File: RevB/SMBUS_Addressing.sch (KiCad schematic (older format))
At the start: 16 parts, among them SW1 SW_DIP_x03, SW2 SW_DIP_x04, SW3 SW_DIP_x03, U3 4051

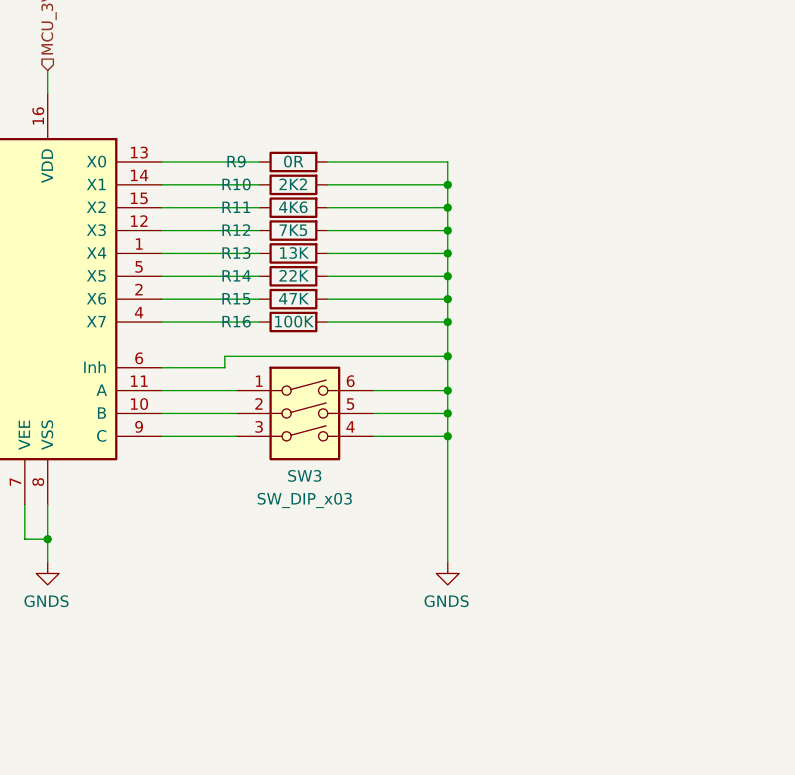
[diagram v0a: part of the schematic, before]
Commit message: updated revb
added missing pullup resistors
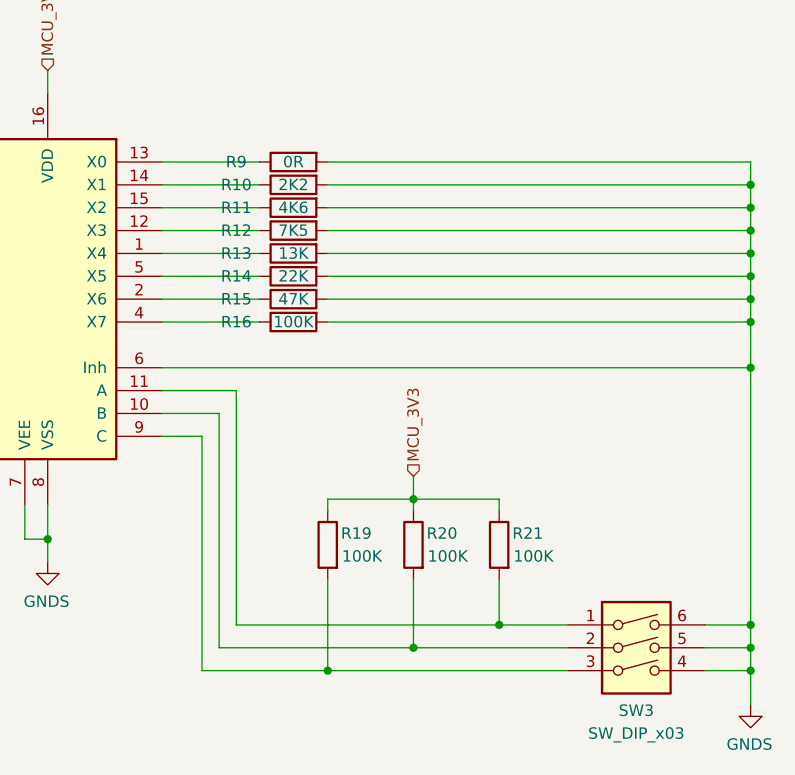
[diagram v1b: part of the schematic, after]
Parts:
- added R19, R20, R21: 100K, Resistor_SMD:R_0805_2012Metric_Pad1.15x1.40mm_HandSolder, symbol Device:R
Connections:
- net MCU_3V3: now also R19.1, R20.1, R21.1
- net at SW3.1, U3.11 (A): now also R21.2
- net at SW3.2, U3.10 (B): now also R20.2
- net at SW3.3, U3.9 (C): now also R19.2
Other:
- moved on the sheet: SW3
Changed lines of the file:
@@
 F 1 "4051" H 6094 4330 50  0000 L CNN
 F 2 "Package_SO:SOIC-16_3.9x9.9mm_P1.27mm" H 5550 4375 50  0001 C CNN
-F 3 "http://www.intersil.com/content/dam/Intersil/documents/cd40/cd4051bms-52bms-53bms.pdf" H 5550 4375 50  0001 C CNN
+F 3 "https://www.ti.com/lit/ds/symlink/cd4052b.pdf?ts=1595798534897&ref_url=https%253A%252F%252Fwww.google.com%252F" H 5550 4375 50  0001 C CNN
 	1    5550 4375
 	-1   0    0    -1
@@
 Wire Wire Line
 	5550 5425 5550 5525
-Wire Wire Line
-	6375 4775 6050 4775
-Wire Wire Line
-	6050 4875 6375 4875
-Wire Wire Line
-	6375 4975 6050 4975
 $Comp
 L power:GNDS #PWR?
 U 1 1 5F3F82F4
-P 7300 5525
+P 8625 6150
 AR Path="/5EFF0F4B/5F3F82F4" Ref="#PWR?"  Part="1"
 AR Path="/5F02F4E9/5F3E7977/5F3F82F4" Ref="#PWR08"  Part="1"
 AR Path="/5F02F4E9/5F4AA6E5/5F3F82F4" Ref="#PWR013"  Part="1"
-F 0 "#PWR013" H 7300 5275 50  0001 C CNN
-F 1 "GNDS" H 7305 5352 50  0000 C CNN
-F 2 "" H 7300 5525 50  0001 C CNN
-F 3 "" H 7300 5525 50  0001 C CNN
-	1    7300 5525
-	-1   0    0    -1
-$EndComp
-Wire Wire Line
-	7300 4975 6975 4975
-Wire Wire Line
-	6975 4875 7300 4875
-Wire Wire Line
-	7300 4875 7300 4975
-Connection ~ 7300 4975
-Wire Wire Line
-	7300 4975 7300 5525
-Wire Wire Line
-	6975 4775 7300 4775
-Wire Wire Line
-	7300 4775 7300 4875
-Connection ~ 7300 4875
-Connection ~ 7300 4775
+F 0 "#PWR013" H 8625 5900 50  0001 C CNN
+F 1 "GNDS" H 8630 5977 50  0000 C CNN
+F 2 "" H 8625 6150 50  0001 C CNN
+F 3 "" H 8625 6150 50  0001 C CNN
+	1    8625 6150
+	-1   0    0    -1
+$EndComp
 $Comp
 L Device:R R?
@@
 	6475 4475 6050 4475
 Wire Wire Line
-	6775 4475 7300 4475
+	6775 4475 8625 4475
 $Comp
 L Device:R R?
@@
 	6475 4375 6050 4375
 Wire Wire Line
-	6775 4375 7300 4375
+	6775 4375 8625 4375
 $Comp
 L Device:R R?
@@
 	6475 4275 6050 4275
 Wire Wire Line
-	6775 4275 7300 4275
+	6775 4275 8625 4275
 $Comp
 L Device:R R?
@@
 	6475 4175 6050 4175
 Wire Wire Line
-	6775 4175 7300 4175
+	6775 4175 8625 4175
 $Comp
 L Device:R R?
@@
 	6475 4075 6050 4075
 Wire Wire Line
-	6775 4075 7300 4075
+	6775 4075 8625 4075
 $Comp
 L Device:R R?
@@
 	6475 3975 6050 3975
 Wire Wire Line
-	6775 3975 7300 3975
+	6775 3975 8625 3975
 $Comp
 L Device:R R?
@@
 	6475 3875 6050 3875
 Wire Wire Line
-	6775 3875 7300 3875
+	6775 3875 8625 3875
 $Comp
 L Device:R R?
@@
 	6475 3775 6050 3775
 Wire Wire Line
-	6775 3775 7300 3775
-Wire Wire Line
-	7300 3775 7300 3875
-Connection ~ 7300 3875
-Wire Wire Line
-	7300 3875 7300 3975
-Connection ~ 7300 3975
-Wire Wire Line
-	7300 3975 7300 4075
-Connection ~ 7300 4075
-Wire Wire Line
-	7300 4075 7300 4175
-Connection ~ 7300 4175
-Wire Wire Line
-	7300 4175 7300 4275
-Connection ~ 7300 4275
-Wire Wire Line
-	7300 4275 7300 4375
-Connection ~ 7300 4375
-Wire Wire Line
-	7300 4375 7300 4475
-Connection ~ 7300 4475
+	6775 3775 8625 3775
+Wire Wire Line
+	8625 3775 8625 3875
+Connection ~ 8625 3875
+Wire Wire Line
+	8625 3875 8625 3975
+Connection ~ 8625 3975
+Wire Wire Line
+	8625 3975 8625 4075
+Connection ~ 8625 4075
+Wire Wire Line
+	8625 4075 8625 4175
+Connection ~ 8625 4175
+Wire Wire Line
+	8625 4175 8625 4275
+Connection ~ 8625 4275
+Wire Wire Line
+	8625 4275 8625 4375
+Connection ~ 8625 4375
+Wire Wire Line
+	8625 4375 8625 4475
+Connection ~ 8625 4475
 Text HLabel 2650 3225 0    50   Input ~ 0
 SMBUS_ADDR2
@@
 	1    0    0    -1
 $EndComp
-Wire Wire Line
-	6050 4675 6325 4675
-Wire Wire Line
-	6325 4675 6325 4625
 $Comp
 L Switch:SW_DIP_x03 SW3
 U 1 1 5F2BCE96
-P 6675 4975
-F 0 "SW3" H 6675 4800 50  0000 C CNN
-F 1 "SW_DIP_x03" H 6675 4700 50  0000 C CNN
-F 2 "Button_Switch_SMD:SW_DIP_SPSTx03_Slide_6.7x9.18mm_W8.61mm_P2.54mm_LowProfile" H 6675 4975 50  0001 C CNN
-F 3 "~" H 6675 4975 50  0001 C CNN
-	1    6675 4975
+P 8125 6000
+F 0 "SW3" H 8125 5825 50  0000 C CNN
+F 1 "SW_DIP_x03" H 8125 5725 50  0000 C CNN
+F 2 "Button_Switch_SMD:SW_DIP_SPSTx03_Slide_6.7x9.18mm_W8.61mm_P2.54mm_LowProfile" H 8125 6000 50  0001 C CNN
+F 3 "~" H 8125 6000 50  0001 C CNN
+	1    8125 6000
 	1    0    0    -1
 $EndComp
 Wire Wire Line
-	7300 4475 7300 4625
-Wire Wire Line
-	6325 4625 7300 4625
-Connection ~ 7300 4625
-Wire Wire Line
-	7300 4625 7300 4775
+	8625 4475 8625 4675
+Connection ~ 8625 4675
 $Comp
 L Connector:TestPoint TP?
@@
 	1    0    0    -1
 $EndComp
+Wire Wire Line
+	6050 4775 6375 4775
+Wire Wire Line
+	6375 4775 6375 5800
+Wire Wire Line
+	6375 5800 7525 5800
+Wire Wire Line
+	6050 4875 6300 4875
+Wire Wire Line
+	6300 4875 6300 5900
+Wire Wire Line
+	6300 5900 7150 5900
+Wire Wire Line
+	6050 4975 6225 4975
+Wire Wire Line
+	6225 4975 6225 6000
+Wire Wire Line
+	6225 6000 6775 6000
+Wire Wire Line
+	6050 4675 8625 4675
+$Comp
+L Device:R R?
+U 1 1 5F442CB6
+P 7525 5450
+AR Path="/5EFF0F4B/5F442CB6" Ref="R?"  Part="1"
+AR Path="/5F02F4E9/5F442CB6" Ref="R?"  Part="1"
+AR Path="/5F02F4E9/5F3E7977/5F442CB6" Ref="R?"  Part="1"
+AR Path="/5F02F4E9/5F4AA6E5/5F442CB6" Ref="R21"  Part="1"
+F 0 "R21" H 7400 5500 50  0000 C CNN
+F 1 "100K" H 7375 5400 50  0000 C CNN
+F 2 "Resistor_SMD:R_0805_2012Metric_Pad1.15x1.40mm_HandSolder" V 7455 5450 50  0001 C CNN
+F 3 "~" H 7525 5450 50  0001 C CNN
+	1    7525 5450
+	-1   0    0    -1
+$EndComp
+Connection ~ 8625 5800
+Wire Wire Line
+	8625 5800 8625 5900
+Connection ~ 8625 5900
+Wire Wire Line
+	8625 5900 8625 6000
+Connection ~ 8625 6000
+Wire Wire Line
+	8625 6000 8625 6150
+Wire Wire Line
+	8625 4675 8625 5800
+Wire Wire Line
+	7525 5250 7525 5300
+Wire Wire Line
+	7525 5600 7525 5800
+Text HLabel 7150 5150 1    50   Input ~ 0
+MCU_3V3
+$Comp
+L Device:R R?
+U 1 1 5F4614AE
+P 7150 5450
+AR Path="/5EFF0F4B/5F4614AE" Ref="R?"  Part="1"
+AR Path="/5F02F4E9/5F4614AE" Ref="R?"  Part="1"
+AR Path="/5F02F4E9/5F3E7977/5F4614AE" Ref="R?"  Part="1"
+AR Path="/5F02F4E9/5F4AA6E5/5F4614AE" Ref="R20"  Part="1"
+F 0 "R20" H 7025 5500 50  0000 C CNN
+F 1 "100K" H 7000 5400 50  0000 C CNN
+F 2 "Resistor_SMD:R_0805_2012Metric_Pad1.15x1.40mm_HandSolder" V 7080 5450 50  0001 C CNN
+F 3 "~" H 7150 5450 50  0001 C CNN
+	1    7150 5450
+	-1   0    0    -1
+$EndComp
+Wire Wire Line
+	7150 5150 7150 5250
+$Comp
+L Device:R R?
+U 1 1 5F464BEE
+P 6775 5450
+AR Path="/5EFF0F4B/5F464BEE" Ref="R?"  Part="1"
+AR Path="/5F02F4E9/5F464BEE" Ref="R?"  Part="1"
+AR Path="/5F02F4E9/5F3E7977/5F464BEE" Ref="R?"  Part="1"
+AR Path="/5F02F4E9/5F4AA6E5/5F464BEE" Ref="R19"  Part="1"
+F 0 "R19" H 6650 5500 50  0000 C CNN
+F 1 "100K" H 6625 5400 50  0000 C CNN
+F 2 "Resistor_SMD:R_0805_2012Metric_Pad1.15x1.40mm_HandSolder" V 6705 5450 50  0001 C CNN
+F 3 "~" H 6775 5450 50  0001 C CNN
+	1    6775 5450
+	-1   0    0    -1
+$EndComp
+Wire Wire Line
+	7150 5600 7150 5900
+Wire Wire Line
+	6775 5600 6775 6000
+Wire Wire Line
+	7525 5250 7150 5250
+Wire Wire Line
+	6775 5250 6775 5300
+Connection ~ 7150 5250
+Wire Wire Line
+	7150 5250 7150 5300
+Wire Wire Line
+	7150 5250 6775 5250
+Wire Wire Line
+	8425 5900 8625 5900
+Wire Wire Line
+	8425 5800 8625 5800
+Wire Wire Line
+	8425 6000 8625 6000
+Connection ~ 6775 6000
+Wire Wire Line
+	6775 6000 7825 6000
+Connection ~ 7150 5900
+Wire Wire Line
+	7150 5900 7825 5900
+Connection ~ 7525 5800
+Wire Wire Line
+	7525 5800 7825 5800
 $EndSCHEMATC

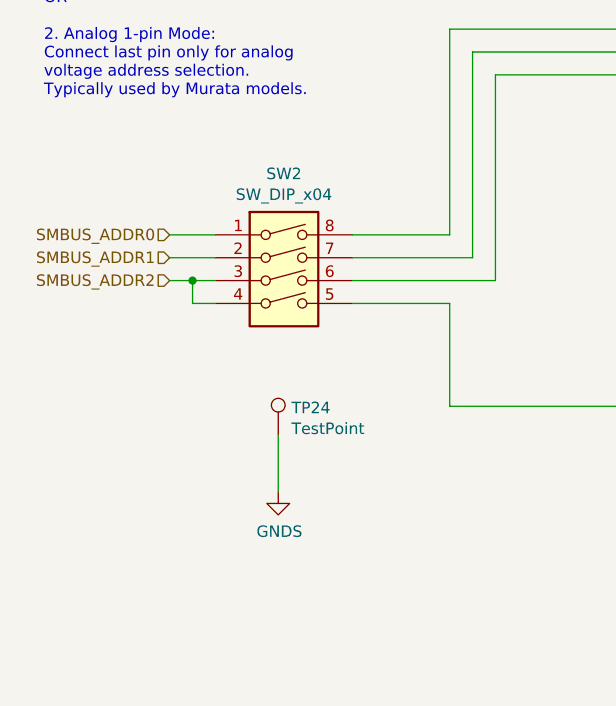
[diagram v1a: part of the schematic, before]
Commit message: hw update
- Reduced RevB layout dimensions
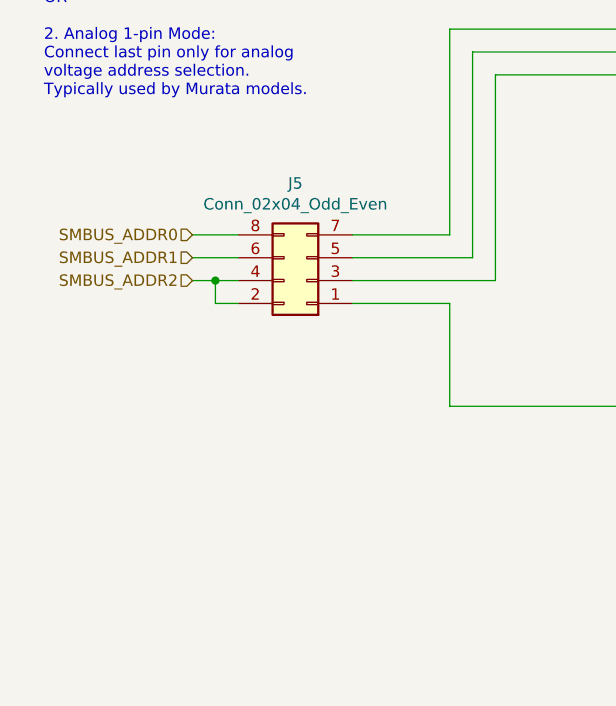
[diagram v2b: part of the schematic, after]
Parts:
- removed SW2: SW_DIP_x04, Button_Switch_SMD:SW_DIP_SPSTx04_Slide_6.7x11.72mm_W8.61mm_P2.54mm_LowProfile, symbol Switch:SW_DIP_x04
- removed TP24: TestPoint, TestPoint:TestPoint_Pad_1.0x1.0mm, symbol Connector:TestPoint
- added J5: Conn_02x04_Odd_Even, Connector_PinHeader_2.54mm:PinHeader_2x04_P2.54mm_Vertical, symbol Connector_Generic:Conn_02x04_Odd_Even
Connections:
- net SMBUS_ADDR0: now also J5.8 (Pin_8)
- net SMBUS_ADDR1: now also J5.6 (Pin_6)
- net SMBUS_ADDR2: now also J5.2 (Pin_2), J5.4 (Pin_4)
- net at U3.3 (X): now also J5.1 (Pin_1)
- net at R8.2, SW1.3: now also J5.3 (Pin_3)
- net at R7.2, SW1.2: now also J5.5 (Pin_5)
- net at R6.2, SW1.1: now also J5.7 (Pin_7)
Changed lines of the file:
@@
 	8625 4375 8625 4475
 Connection ~ 8625 4475
-Text HLabel 2650 3225 0    50   Input ~ 0
+Text HLabel 2750 3225 0    50   Input ~ 0
 SMBUS_ADDR2
-Text HLabel 2650 3125 0    50   Input ~ 0
+Text HLabel 2750 3125 0    50   Input ~ 0
 SMBUS_ADDR1
-Text HLabel 2650 3025 0    50   Input ~ 0
+Text HLabel 2750 3025 0    50   Input ~ 0
 SMBUS_ADDR0
 Text HLabel 5550 3375 1    50   Input ~ 0
@@
 	5550 3375 5550 3475
 Wire Wire Line
-	2650 3025 2850 3025
-Wire Wire Line
-	2650 3125 2850 3125
-Wire Wire Line
-	2650 3225 2750 3225
-Wire Wire Line
-	2850 3325 2750 3325
-Wire Wire Line
-	2750 3325 2750 3225
-Connection ~ 2750 3225
+	2750 3025 2950 3025
+Wire Wire Line
+	2750 3125 2950 3125
 Wire Wire Line
 	2750 3225 2850 3225
+Wire Wire Line
+	2950 3325 2850 3325
+Wire Wire Line
+	2850 3325 2850 3225
+Connection ~ 2850 3225
+Wire Wire Line
+	2850 3225 2950 3225
 Wire Wire Line
 	3450 3325 3875 3325
@@
 $EndComp
 $Comp
-L Switch:SW_DIP_x04 SW2
-U 1 1 5F2ADDB0
-P 3150 3225
-F 0 "SW2" H 3150 3692 50  0000 C CNN
-F 1 "SW_DIP_x04" H 3150 3601 50  0000 C CNN
-F 2 "Button_Switch_SMD:SW_DIP_SPSTx04_Slide_6.7x11.72mm_W8.61mm_P2.54mm_LowProfile" H 3150 3225 50  0001 C CNN
-F 3 "~" H 3150 3225 50  0001 C CNN
-	1    3150 3225
-	1    0    0    -1
-$EndComp
-$Comp
 L Switch:SW_DIP_x03 SW3
 U 1 1 5F2BCE96
@@
 	8625 4475 8625 4675
 Connection ~ 8625 4675
-$Comp
-L Connector:TestPoint TP?
-U 1 1 5F341E88
-P 3125 3900
-AR Path="/5F02F4E9/5F341E88" Ref="TP?"  Part="1"
-AR Path="/5F02F4E9/5F4AA6E5/5F341E88" Ref="TP24"  Part="1"
-F 0 "TP24" H 3183 4018 50  0000 L CNN
-F 1 "TestPoint" H 3183 3927 50  0000 L CNN
-F 2 "TestPoint:TestPoint_Pad_1.0x1.0mm" H 3325 3900 50  0001 C CNN
-F 3 "~" H 3325 3900 50  0001 C CNN
-	1    3125 3900
-	1    0    0    -1
-$EndComp
-Wire Wire Line
-	3125 3900 3125 4150
-$Comp
-L power:GNDS #PWR017
-U 1 1 5F344131
-P 3125 4150
-F 0 "#PWR017" H 3125 3900 50  0001 C CNN
-F 1 "GNDS" H 3130 3977 50  0000 C CNN
-F 2 "" H 3125 4150 50  0001 C CNN
-F 3 "" H 3125 4150 50  0001 C CNN
-	1    3125 4150
-	1    0    0    -1
-$EndComp
 Wire Wire Line
 	6050 4775 6375 4775
@@
 Wire Wire Line
 	7525 5800 7825 5800
+$Comp
+L Connector_Generic:Conn_02x04_Odd_Even J5
+U 1 1 5F2E0CB1
+P 3250 3225
+F 0 "J5" H 3300 2800 50  0000 C CNN
+F 1 "Conn_02x04_Odd_Even" H 3300 2891 50  0000 C CNN
+F 2 "Connector_PinHeader_2.54mm:PinHeader_2x04_P2.54mm_Vertical" H 3250 3225 50  0001 C CNN
+F 3 "~" H 3250 3225 50  0001 C CNN
+	1    3250 3225
+	-1   0    0    1
+$EndComp
 $EndSCHEMATC
